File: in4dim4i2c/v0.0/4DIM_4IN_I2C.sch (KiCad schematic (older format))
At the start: 79 parts, among them IC1 ATTINY2313-P, IC2 MOC3020M, IC3 MOC3020M, IC4 MOC3020M, IC5 MOC3020M, IC6 P620, P1 CONN_2, P10 CONN_2, P2 CONN_2, P3 CONN_2, P4 CONN_5, P5 CONN_5, P6 CONN_5, P7 CONN_2, P8 CONN_2, P9 CONN_2, U1 TRIAC, U2 TRIAC, U3 TRIAC, U4 TRIAC

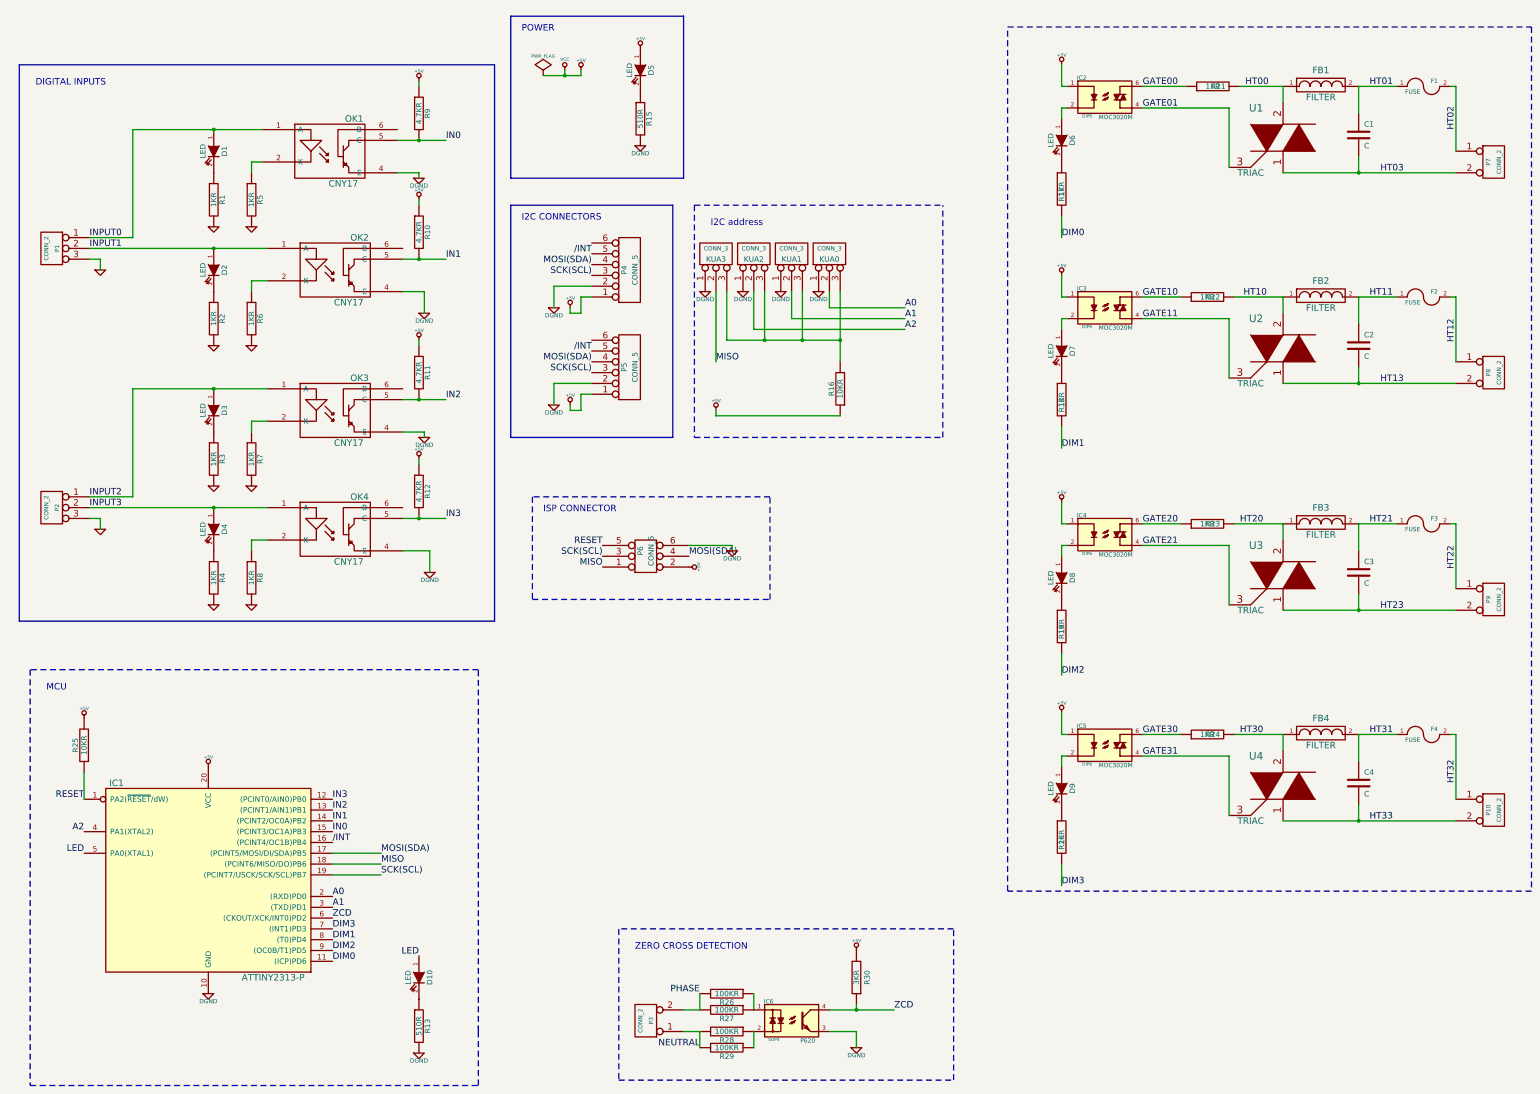
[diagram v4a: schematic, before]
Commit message: Change the footprint of Triac (inverted)
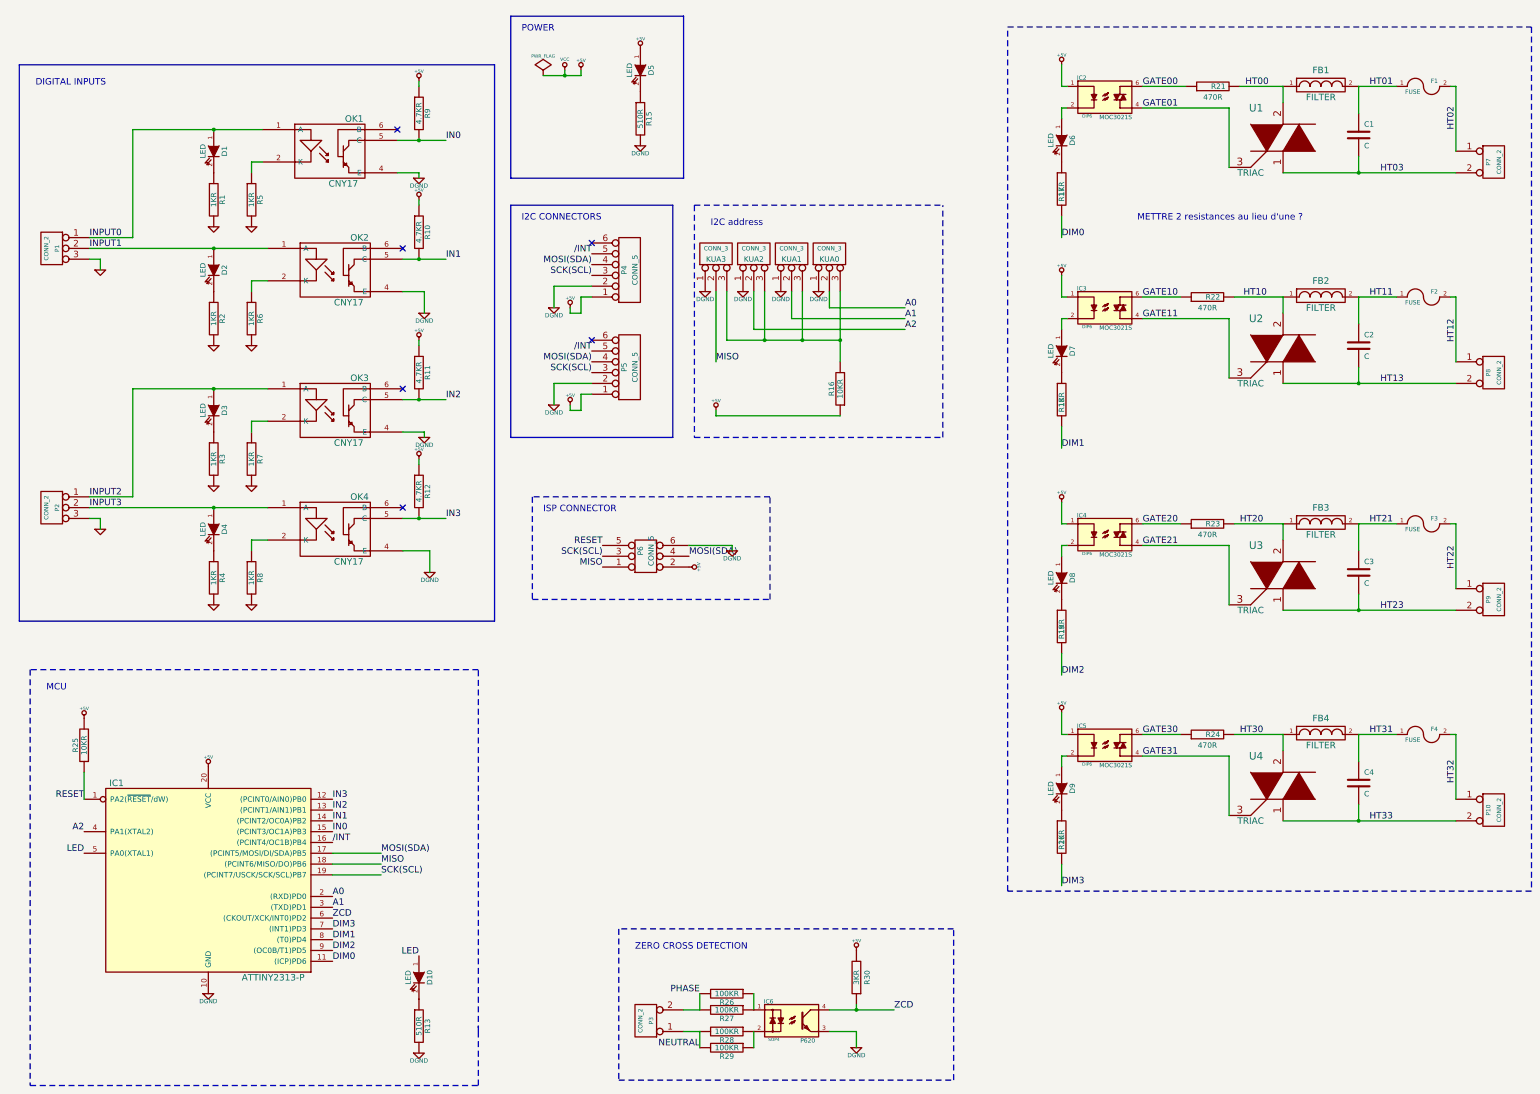
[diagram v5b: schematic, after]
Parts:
- IC2, IC3, IC4, IC5: value MOC3020M -> MOC3021S
- R21, R22, R23, R24: value 1KR -> 470R
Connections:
- no-connect marks 0 -> 6
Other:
- note added: "METTRE 2 resistances au lieu d'une ?"
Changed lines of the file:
@@
-EESchema Schematic File Version 2  date mer. 29 août 2012 22:06:22 CEST
+EESchema Schematic File Version 2  date ven. 31 août 2012 21:57:51 CEST
 LIBS:power
 LIBS:device
@@
 Sheet 1 1
 Title "16 Digital Inputs Multiplexied Board"
-Date "29 aug 2012"
+Date "31 aug 2012"
 Rev "draft"
 Comp "XPLDUINO project"
@@
 P 11000 1350
 F 0 "IC2" H 10786 1529 40  0000 C CNN
-F 1 "MOC3020M" H 11100 1165 40  0000 C CNN
+F 1 "MOC3021S" H 11100 1165 40  0000 C CNN
 F 2 "DIP6" H 10836 1175 29  0000 C CNN
 	1    11000 1350
@@
 P 12000 1250
 F 0 "R21" V 12000 1200 50  0000 C CNN
-F 1 "1KR" V 12000 1250 50  0000 C CNN
+F 1 "470R" V 11900 1250 50  0000 C CNN
 	1    12000 1250
 	0    -1   -1   0
@@
 P 11000 3300
 F 0 "IC3" H 10786 3479 40  0000 C CNN
-F 1 "MOC3020M" H 11100 3115 40  0000 C CNN
+F 1 "MOC3021S" H 11100 3115 40  0000 C CNN
 F 2 "DIP6" H 10836 3125 29  0000 C CNN
 	1    11000 3300
@@
 P 11950 3200
 F 0 "R22" V 11950 3150 50  0000 C CNN
-F 1 "1KR" V 11950 3200 50  0000 C CNN
+F 1 "470R" V 11850 3200 50  0000 C CNN
 	1    11950 3200
 	0    -1   -1   0
@@
 P 11000 5400
 F 0 "IC4" H 10786 5579 40  0000 C CNN
-F 1 "MOC3020M" H 11100 5215 40  0000 C CNN
+F 1 "MOC3021S" H 11100 5215 40  0000 C CNN
 F 2 "DIP6" H 10836 5225 29  0000 C CNN
 	1    11000 5400
@@
 P 11950 5300
 F 0 "R23" V 11950 5250 50  0000 C CNN
-F 1 "1KR" V 11950 5300 50  0000 C CNN
+F 1 "470R" V 11850 5300 50  0000 C CNN
 	1    11950 5300
 	0    -1   -1   0
@@
 P 11000 7350
 F 0 "IC5" H 10786 7529 40  0000 C CNN
-F 1 "MOC3020M" H 11100 7165 40  0000 C CNN
+F 1 "MOC3021S" H 11100 7165 40  0000 C CNN
 F 2 "DIP6" H 10836 7175 29  0000 C CNN
 	1    11000 7350
@@
 P 11950 7250
 F 0 "R24" V 11950 7200 50  0000 C CNN
-F 1 "1KR" V 11950 7250 50  0000 C CNN
+F 1 "470R" V 11850 7250 50  0000 C CNN
 	1    11950 7250
 	0    -1   -1   0
@@
 Text Label 7400 3800 0    60   ~ 0
 MISO
+NoConn ~ 4500 5150
+NoConn ~ 4500 4050
+NoConn ~ 4500 2750
+NoConn ~ 4450 1650
+NoConn ~ 6250 3600
+NoConn ~ 6250 2700
+Text Notes 11300 2500 0    60   ~ 0
+METTRE 2 resistances au lieu d'une ?
 $EndSCHEMATC

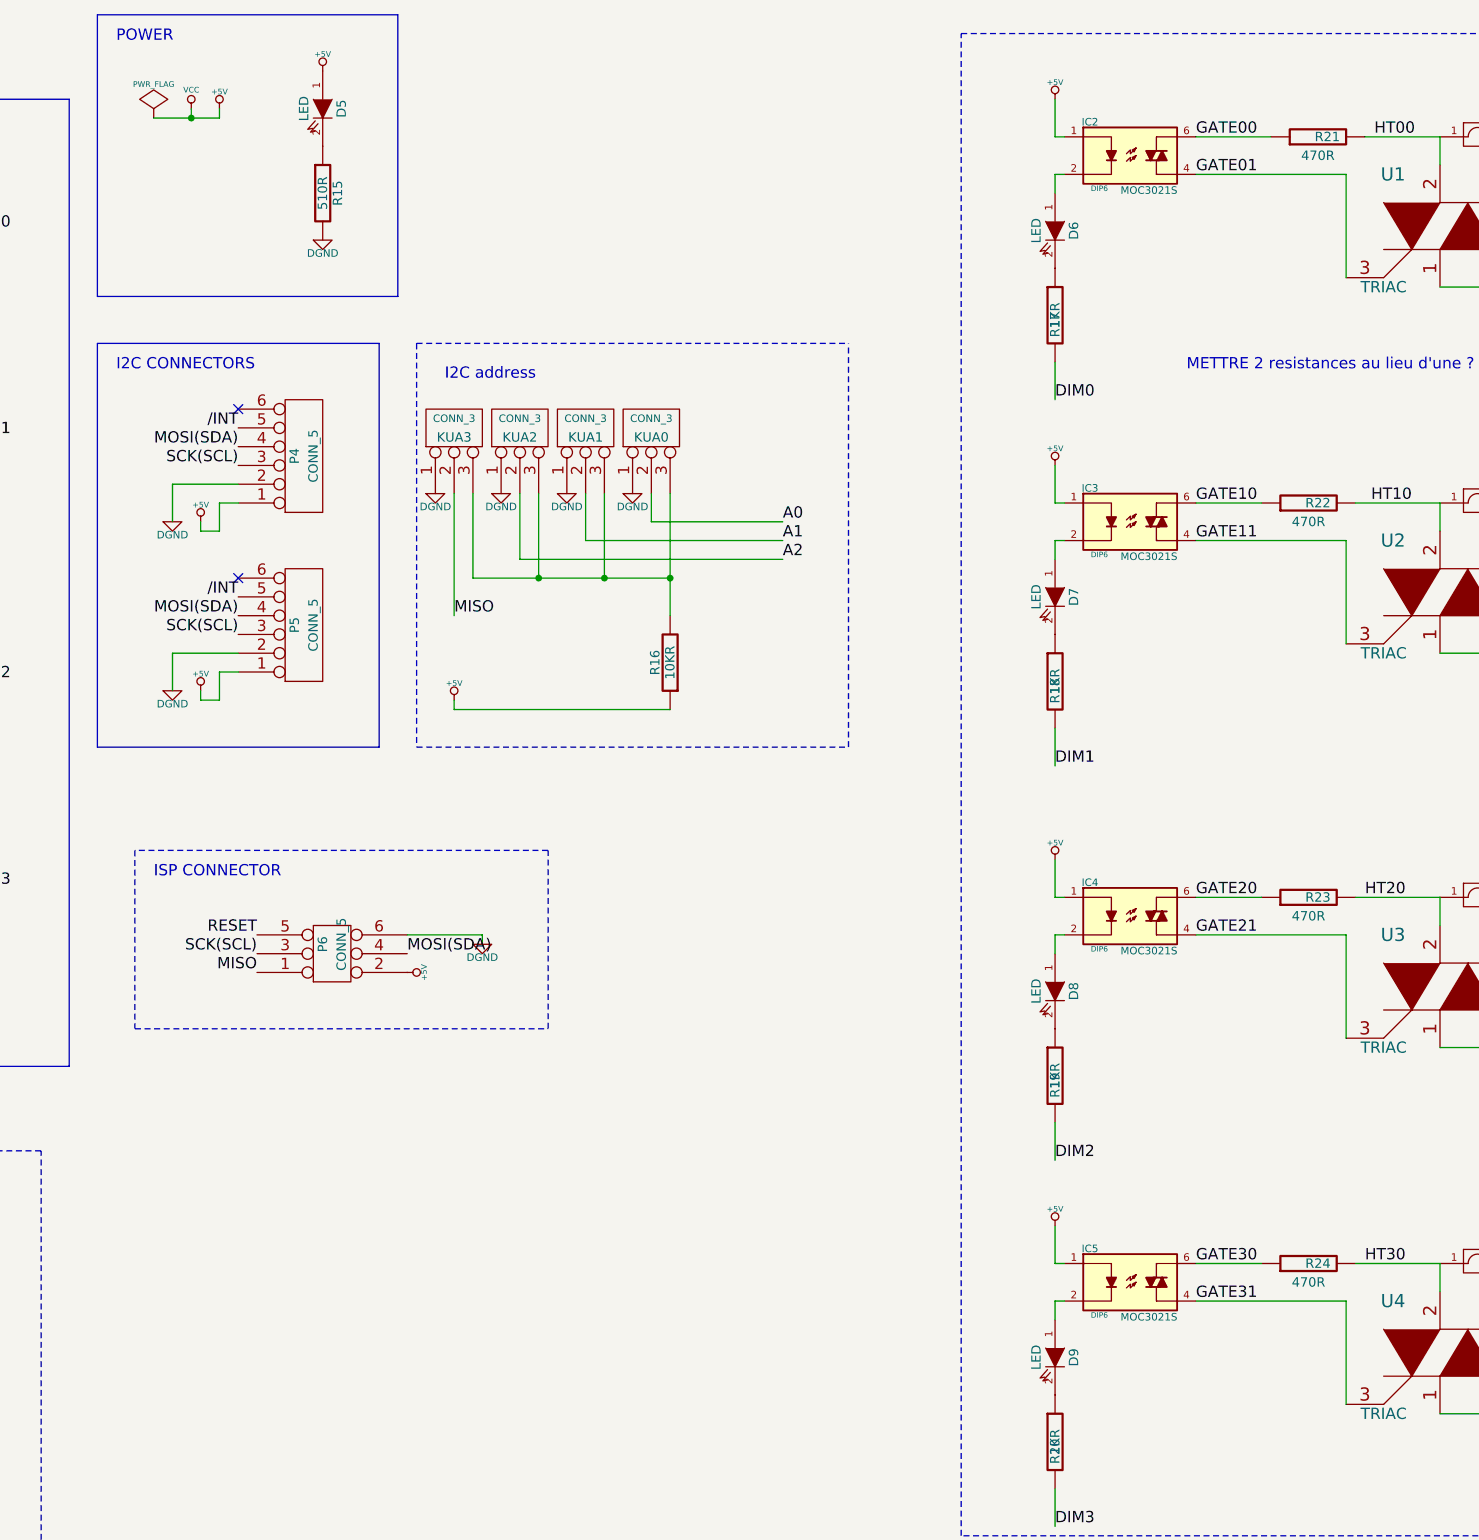
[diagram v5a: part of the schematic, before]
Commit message: Add resistor on the command of triacs Add capacitors on power
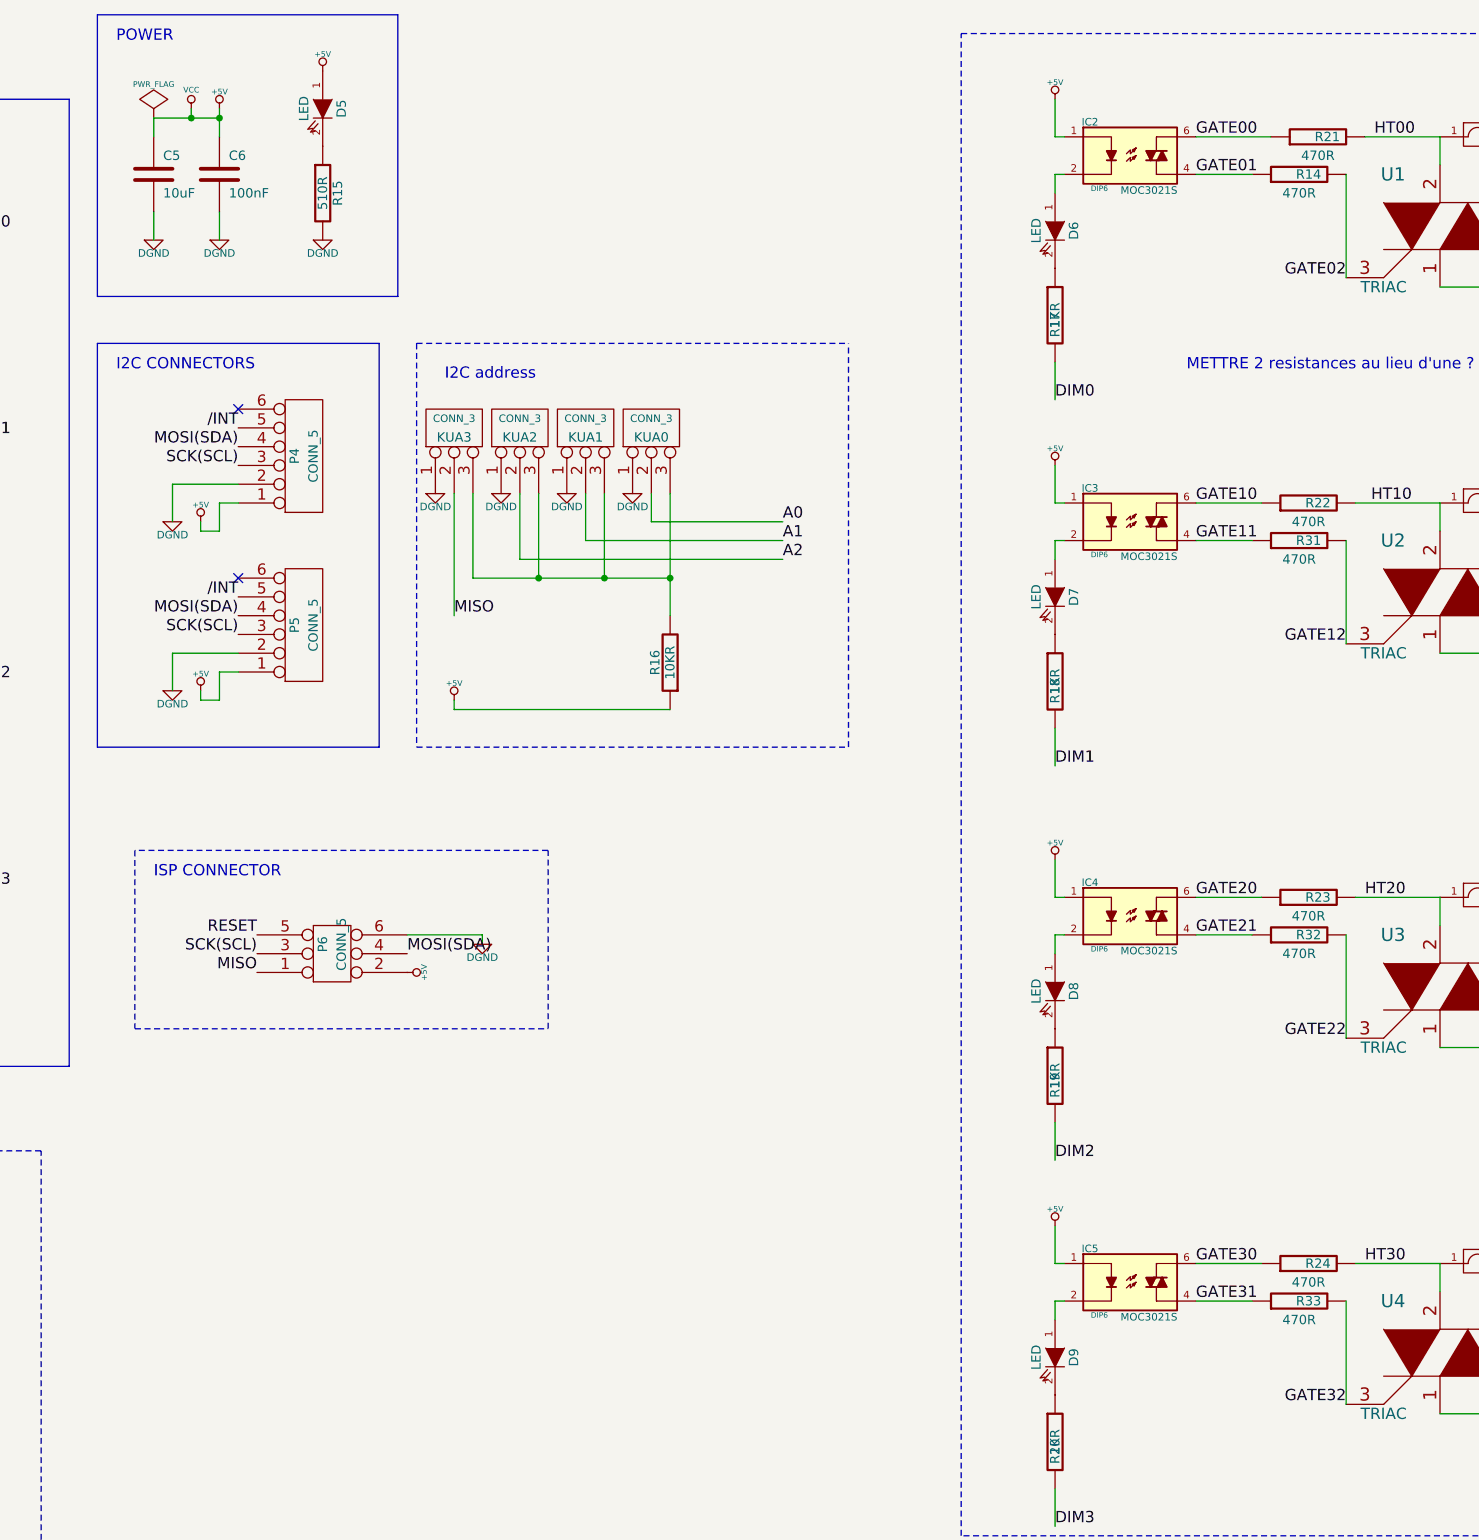
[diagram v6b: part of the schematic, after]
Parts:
- added C5: 10uF, symbol C
- added C6: 100nF, symbol C
- added R14, R31, R32, R33: 470R, symbol R
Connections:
- net +5V: now also C5.1, C6.1
- net DGND: now also C5.2, C6.2
- net GATE01: now also R14.1; no longer U1.3
- net GATE11: now also R31.1; no longer U2.3
- net GATE21: now also R32.1; no longer U3.3
- net GATE31: now also R33.1; no longer U4.3
- new net GATE02: R14.2, U1.3
- new net GATE12: R31.2, U2.3
- new net GATE22: R32.2, U3.3
- new net GATE32: R33.2, U4.3
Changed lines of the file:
@@
-EESchema Schematic File Version 2  date ven. 31 août 2012 21:57:51 CEST
+EESchema Schematic File Version 2  date mer. 05 sept. 2012 22:01:51 CEST
 LIBS:power
 LIBS:device
@@
 Sheet 1 1
 Title "16 Digital Inputs Multiplexied Board"
-Date "31 aug 2012"
+Date "5 sep 2012"
 Rev "draft"
 Comp "XPLDUINO project"
@@
 	6000 1100 6000 1150
 Wire Wire Line
-	6150 1150 6150 1100
+	6150 1100 6150 1250
 Wire Wire Line
 	5800 1150 6150 1150
@@
 	12650 1250 12650 1400
 Wire Wire Line
-	11350 1450 12150 1450
-Wire Wire Line
 	12150 1450 12150 2000
 Wire Wire Line
@@
 	12650 3200 12650 3350
 Wire Wire Line
-	11350 3400 12150 3400
-Wire Wire Line
 	12150 3400 12150 3950
 Wire Wire Line
@@
 	12650 5300 12650 5450
 Wire Wire Line
-	11350 5500 12150 5500
-Wire Wire Line
 	12150 5500 12150 6050
 Wire Wire Line
@@
 Wire Wire Line
 	12650 7250 12650 7400
-Wire Wire Line
-	11350 7450 12150 7450
 Wire Wire Line
 	12150 7450 12150 8000
@@
 Text Notes 11300 2500 0    60   ~ 0
 METTRE 2 resistances au lieu d'une ?
+$Comp
+L C C5
+U 1 1 50479B33
+P 5800 1450
+F 0 "C5" H 5850 1550 50  0000 L CNN
+F 1 "10uF" H 5850 1350 50  0000 L CNN
+	1    5800 1450
+	1    0    0    -1
+$EndComp
+$Comp
+L C C6
+U 1 1 50479B42
+P 6150 1450
+F 0 "C6" H 6200 1550 50  0000 L CNN
+F 1 "100nF" H 6200 1350 50  0000 L CNN
+	1    6150 1450
+	1    0    0    -1
+$EndComp
+$Comp
+L DGND #PWR045
+U 1 1 50479B59
+P 6150 1800
+F 0 "#PWR045" H 6150 1800 40  0001 C CNN
+F 1 "DGND" H 6150 1730 40  0000 C CNN
+	1    6150 1800
+	1    0    0    -1
+$EndComp
+$Comp
+L DGND #PWR046
+U 1 1 50479B5F
+P 5800 1800
+F 0 "#PWR046" H 5800 1800 40  0001 C CNN
+F 1 "DGND" H 5800 1730 40  0000 C CNN
+	1    5800 1800
+	1    0    0    -1
+$EndComp
+Connection ~ 6150 1150
+Wire Wire Line
+	5800 1150 5800 1250
+Wire Wire Line
+	5800 1650 5800 1800
+Wire Wire Line
+	6150 1650 6150 1800
+$Comp
+L R R14
+U 1 1 5047AB22
+P 11900 1450
+F 0 "R14" V 11900 1400 50  0000 C CNN
+F 1 "470R" V 11800 1450 50  0000 C CNN
+	1    11900 1450
+	0    -1   -1   0
+$EndComp
+Wire Wire Line
+	11350 1450 11650 1450
+Text Label 12150 2000 2    60   ~ 0
+GATE02
+$Comp
+L R R31
+U 1 1 5047ACDA
+P 11900 3400
+F 0 "R31" V 11900 3350 50  0000 C CNN
+F 1 "470R" V 11800 3400 50  0000 C CNN
+	1    11900 3400
+	0    -1   -1   0
+$EndComp
+Text Label 12150 3950 2    60   ~ 0
+GATE12
+Wire Wire Line
+	11350 3400 11650 3400
+$Comp
+L R R32
+U 1 1 5047AE70
+P 11900 5500
+F 0 "R32" V 11900 5450 50  0000 C CNN
+F 1 "470R" V 11800 5500 50  0000 C CNN
+	1    11900 5500
+	0    -1   -1   0
+$EndComp
+Text Label 12150 6050 2    60   ~ 0
+GATE22
+Wire Wire Line
+	11350 5500 11650 5500
+$Comp
+L R R33
+U 1 1 5047AF3F
+P 11900 7450
+F 0 "R33" V 11900 7400 50  0000 C CNN
+F 1 "470R" V 11800 7450 50  0000 C CNN
+	1    11900 7450
+	0    -1   -1   0
+$EndComp
+Text Label 12150 8000 2    60   ~ 0
+GATE32
+Wire Wire Line
+	11350 7450 11650 7450
 $EndSCHEMATC
